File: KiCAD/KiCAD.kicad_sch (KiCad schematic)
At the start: 0 parts

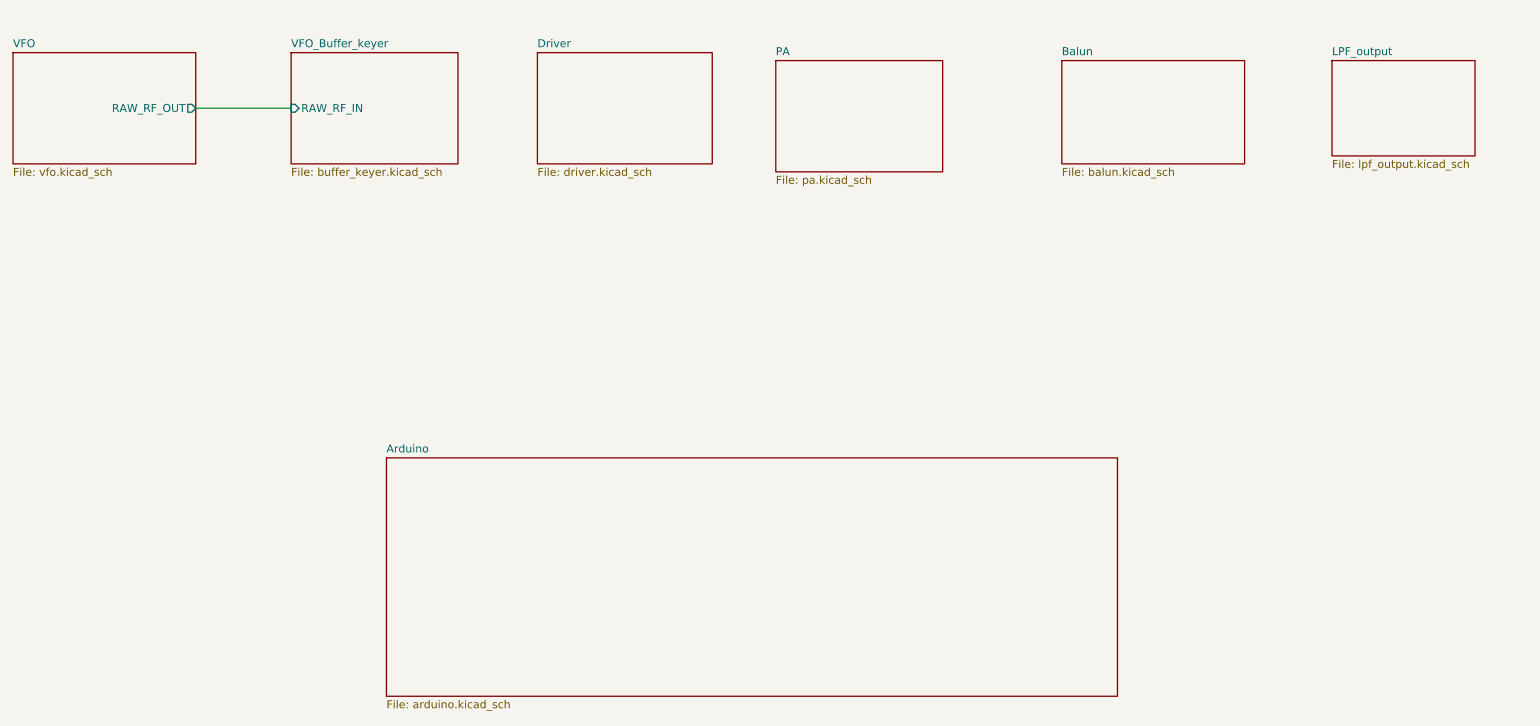
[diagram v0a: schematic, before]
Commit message: kicad(bias): build complete grid-bias sheet (Design A: dual OPA454)
New sheet untitled.kicad_sch (sheet name "Bias", file to be renamed
bias.kicad_sch) implementing the OPA454 high-voltage design per the
Grid_Bias_Schematic.pdf design doc:

- LM7805 (U9) generates the +5 V supply rail from +12 V (~30 mA load,
  no heatsink needed at ~270 mW dissipation)
- LM4040DIZ-5.0 (U11) generates a SEPARATE +5 V_REF precision reference
  biased from +12 V via R_Z = 2.2 kΩ; cathode bypassed by C23 (100 nF).
  Drives only R_GA / R_GB (the two OPA454 summing-junction inputs) and
  the cathode-monitor's 1.5 V threshold divider on its own sheet
- Two OPA454 channels (U5 = Tube A, U10 = Tube B) each with R_F = 170 k,
  R_G = 10 k, R_GL = 22 k, R_pad = 1 k, plus 2N7000 bias-slam (Q2, Q3)
  sharing one R_GATE = 10 k. Transfer function V_out = 18·V_DAC - 85
- Shared bypass caps across U5/U10 V+ and V- rails (1 µF X7R bulk +
  100 nF HF on each rail); justified by grid-bias bandwidth being
  effectively DC vs textbook µV-class instrumentation recommendation

Supporting changes:

- New xmitter:OPA454 multi-unit symbol (Unit A = 3-pin op-amp triangle
  with IN-, IN+, OUT; Unit B = 5-pin power/enable block with V+, V-,
  ED, EDCOMM, STATFLG). Built via tools/add_opa454_symbol.py
- xmitter_prj/grid_bias.sch: V2 = 90 V (was 85), V3 = 5 V (was 12) to
  match the PDF design's +5 V / -90 V supply rails; LM4040 stays at 5 V
- pa_cathode_monitor.md: switch comparator V_REF from the bogus
  LM4040DIZ-1.2 (doesn't exist - LM4040 minimum is 2.048 V) to a shared
  LM4040DIZ-5.0 with a 4.7 k / 1 k trim / 1.5 k divider giving 1.5 V
  nominal (1.21 V to 1.74 V across full pot)
- Documentation/grid_bias.md: full subsystem design doc covering
  architecture decisions, transfer function, per-channel topology, BOM,
  inter-sheet I/O, calibration procedure, and open items
- Documentation/kicad_custom_symbols.md: OPA454 entry plus a note on
  the KiCad sub-symbol naming gotcha (NAME_{unit}_{body_style}, not th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
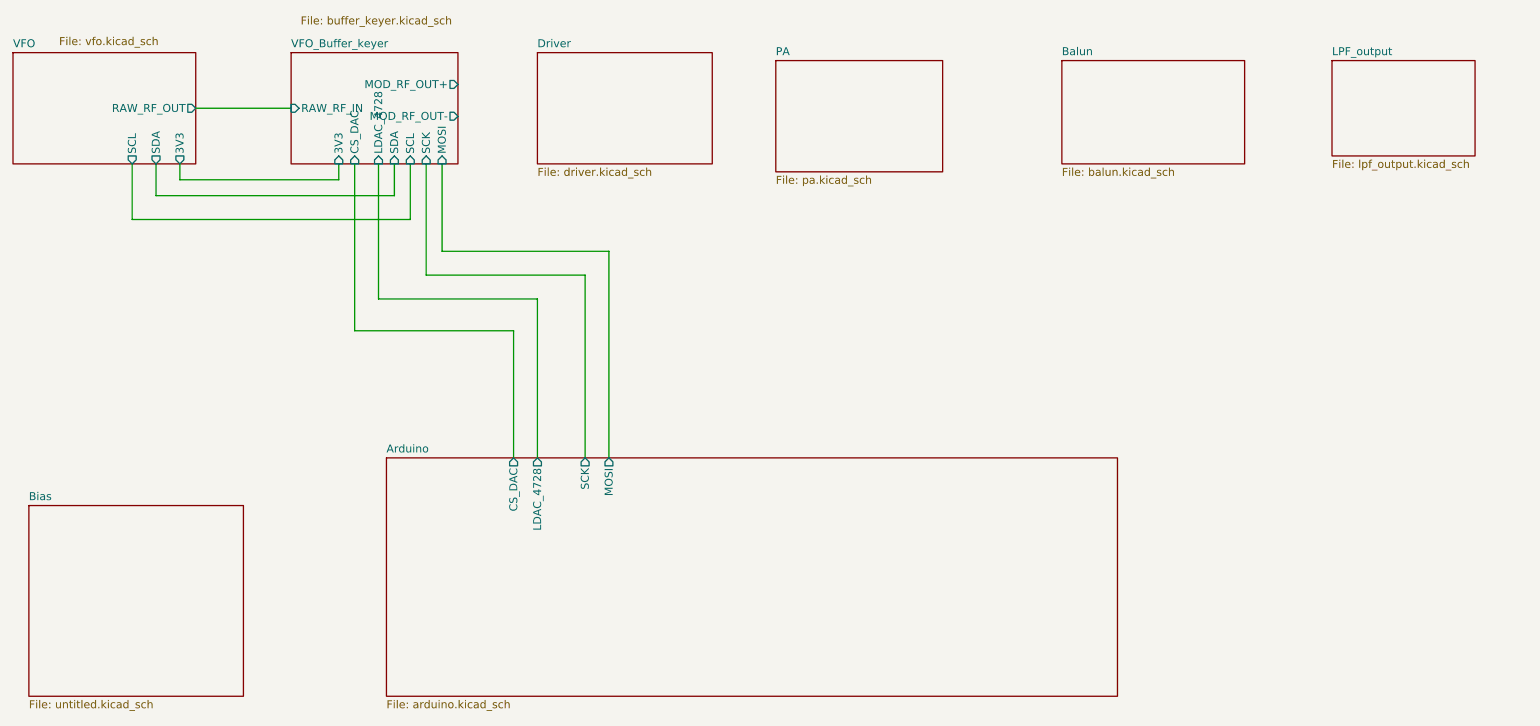
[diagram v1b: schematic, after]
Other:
- added sheet Bias (untitled.kicad_sch)
- sheet Arduino ports: added CS_DAC, LDAC_4728, MOSI, SCK; removed none
- sheet VFO ports: added 3V3, SCL, SDA; removed none
- sheet VFO_Buffer_keyer ports: added 3V3, CS_DAC, LDAC_4728, MOD_RF_OUT+, MOD_RF_OUT-, MOSI, SCK, SCL, SDA; removed none
